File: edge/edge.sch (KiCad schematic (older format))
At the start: 13 parts

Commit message: edge boards
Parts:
- removed D? (x3): LED, ~, symbol LED
- removed R? (x3): R, ~, symbol R
- added C2, C3, C4, C6, C7, C8, C9: 0.1uF, ~, symbol C
- added C5: 2.2uF, ~, symbol C
- added L1: INDUCTOR, ~, symbol INDUCTOR
- added P3: CONN_5, ~, symbol CONN_5
- added P4: CONN_6, ~, symbol CONN_6
- added P5: CONN_3X2, ~, symbol CONN_3X2
- added R1, R2, R3: 22R, ~, symbol R
- gave numbers to parts that had none: 7
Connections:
- net labels added: MISO, MOSI, PA0, PA2, SCK, \RESET
- wire segments 42 -> 76
- no-connect marks 0 -> 4

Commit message: Last version before ATtiny24A
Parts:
- added R4, R5: 10K, ~, symbol R
- added R6, R7, R8: R, ~, symbol R
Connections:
- net labels added: BTN1, BTN1C, BTN2, BTN2C, PB2, PB4
- net labels removed: PA0
- wire segments 76 -> 89
- no-connect marks 4 -> 1

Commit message: ATtiny24A based edge board
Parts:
- removed C5: 2.2uF, ~, symbol C
- removed C6, C7, C8, C9: 0.1uF, ~, symbol C
- removed IC1: ATTINY861A-S, SO20, symbol ATTINY861A-S
- removed P4: CONN_6, ~, symbol CONN_6
- removed Q1, Q2, Q3: MOSFET_N, ~, symbol MOSFET_N
- removed R4, R5: 10K, ~, symbol R
- removed R8: R, ~, symbol R
- added IC1: ATTINY24A-SS, SO14, symbol ATTINY24A-SS
- added Q1, Q2, Q3: NPN, ~, symbol NPN
- added R3: 10K, ~, symbol R
- C2, C4: value 0.1uF -> 10uF
- C3: value 0.1uF -> 1uF
- R1: value 22R -> 170R
- R4: renamed from R2; value 22R -> 170R
- R6, R7: value R -> 10K
- R8: renamed from R3; value 22R -> 170R
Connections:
- net labels added: BB, BLUEP, GB, GREENP, RB, REDP
- net labels removed: PA2, PB2, PB4
- wire segments 89 -> 71
- no-connect marks 1 -> 0

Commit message: Game of Life edge board rerouting
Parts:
- added C5, C6: C, ~, symbol C
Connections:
- wire segments 71 -> 78
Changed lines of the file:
@@
-EESchema Schematic File Version 2  date Sun 05 May 2013 09:03:02 PM EDT
+EESchema Schematic File Version 2  date Sat 11 May 2013 07:52:54 PM EDT
 LIBS:power
 LIBS:device
@@
 Sheet 1 1
 Title ""
-Date "6 may 2013"
+Date "11 may 2013"
 Rev ""
 Comp ""
@@
 $EndComp
 $Comp
-L GND #PWR01
+L GND #PWR10
 U 1 1 512EAE5B
 P 3700 5100
-F 0 "#PWR01" H 3700 5100 30  0001 C CNN
+F 0 "#PWR10" H 3700 5100 30  0001 C CNN
 F 1 "GND" H 3700 5030 30  0001 C CNN
 F 2 "" H 3700 5100 60  0000 C CNN
@@
 $EndComp
 $Comp
-L +3.3V #PWR02
+L +3.3V #PWR12
 U 1 1 512EAE7E
 P 3800 4900
-F 0 "#PWR02" H 3800 4860 30  0001 C CNN
+F 0 "#PWR12" H 3800 4860 30  0001 C CNN
 F 1 "+3.3V" H 3800 5010 30  0000 C CNN
 F 2 "" H 3800 4900 60  0000 C CNN
@@
 $EndComp
 $Comp
-L +12V #PWR03
+L +12V #PWR11
 U 1 1 512EAEA3
 P 3800 4800
-F 0 "#PWR03" H 3800 4750 20  0001 C CNN
+F 0 "#PWR11" H 3800 4750 20  0001 C CNN
 F 1 "+12V" H 3800 4900 30  0000 C CNN
 F 2 "" H 3800 4800 60  0000 C CNN
@@
 $EndComp
 $Comp
-L GND #PWR04
+L GND #PWR17
 U 1 1 512EAF89
 P 4750 5150
-F 0 "#PWR04" H 4750 5150 30  0001 C CNN
+F 0 "#PWR17" H 4750 5150 30  0001 C CNN
 F 1 "GND" H 4750 5080 30  0001 C CNN
 F 2 "" H 4750 5150 60  0000 C CNN
@@
 $EndComp
 $Comp
-L +3.3V #PWR05
+L +3.3V #PWR20
 U 1 1 512EAF91
 P 4850 4950
-F 0 "#PWR05" H 4850 4910 30  0001 C CNN
+F 0 "#PWR20" H 4850 4910 30  0001 C CNN
 F 1 "+3.3V" H 4850 5060 30  0000 C CNN
 F 2 "" H 4850 4950 60  0000 C CNN
@@
 $EndComp
 $Comp
-L +12V #PWR06
+L +12V #PWR19
 U 1 1 512EAF98
 P 4850 4850
-F 0 "#PWR06" H 4850 4800 20  0001 C CNN
+F 0 "#PWR19" H 4850 4800 20  0001 C CNN
 F 1 "+12V" H 4850 4950 30  0000 C CNN
 F 2 "" H 4850 4850 60  0000 C CNN
@@
 INCCW2
 $Comp
-L GND #PWR07
+L GND #PWR9
 U 1 1 512EB1D0
 P 3550 7200
-F 0 "#PWR07" H 3550 7200 30  0001 C CNN
+F 0 "#PWR9" H 3550 7200 30  0001 C CNN
 F 1 "GND" H 3550 7130 30  0001 C CNN
 F 2 "" H 3550 7200 60  0000 C CNN
@@
 RED
 $Comp
-L GND #PWR08
+L GND #PWR15
 U 1 1 512EB27D
 P 4300 7200
-F 0 "#PWR08" H 4300 7200 30  0001 C CNN
+F 0 "#PWR15" H 4300 7200 30  0001 C CNN
 F 1 "GND" H 4300 7130 30  0001 C CNN
 F 2 "" H 4300 7200 60  0000 C CNN
@@
 $EndComp
 $Comp
-L GND #PWR09
+L GND #PWR21
 U 1 1 512EB2B8
 P 5250 7200
-F 0 "#PWR09" H 5250 7200 30  0001 C CNN
+F 0 "#PWR21" H 5250 7200 30  0001 C CNN
 F 1 "GND" H 5250 7130 30  0001 C CNN
 F 2 "" H 5250 7200 60  0000 C CNN
@@
 $EndComp
 $Comp
-L +12V #PWR010
+L +12V #PWR13
 U 1 1 5183CE12
 P 4000 5750
-F 0 "#PWR010" H 4000 5700 20  0001 C CNN
+F 0 "#PWR13" H 4000 5700 20  0001 C CNN
 F 1 "+12V" H 4000 5850 30  0000 C CNN
 F 2 "" H 4000 5750 60  0000 C CNN
@@
 $EndComp
 $Comp
-L +12V #PWR011
+L +12V #PWR16
 U 1 1 5183E9DB
 P 4700 5750
-F 0 "#PWR011" H 4700 5700 20  0001 C CNN
+F 0 "#PWR16" H 4700 5700 20  0001 C CNN
 F 1 "+12V" H 4700 5850 30  0000 C CNN
 F 2 "" H 4700 5750 60  0000 C CNN
@@
 $EndComp
 $Comp
-L VCC #PWR012
+L VCC #PWR2
 U 1 1 5186E69A
 P 1300 900
-F 0 "#PWR012" H 1300 1000 30  0001 C CNN
+F 0 "#PWR2" H 1300 1000 30  0001 C CNN
 F 1 "VCC" H 1300 1000 30  0000 C CNN
 F 2 "" H 1300 900 60  0000 C CNN
@@
 $EndComp
 $Comp
-L GND #PWR013
+L GND #PWR3
 U 1 1 5186E6E5
 P 1300 2300
-F 0 "#PWR013" H 1300 2300 30  0001 C CNN
+F 0 "#PWR3" H 1300 2300 30  0001 C CNN
 F 1 "GND" H 1300 2230 30  0001 C CNN
 F 2 "" H 1300 2300 60  0000 C CNN
@@
 $EndComp
 $Comp
-L GND #PWR014
+L GND #PWR1
 U 1 1 5186F52B
 P 700 1000
-F 0 "#PWR014" H 700 1000 30  0001 C CNN
+F 0 "#PWR1" H 700 1000 30  0001 C CNN
 F 1 "GND" H 700 930 30  0001 C CNN
 F 2 "" H 700 1000 60  0000 C CNN
@@
 $EndComp
 $Comp
-L VCC #PWR015
+L VCC #PWR14
 U 1 1 51870416
 P 4200 2400
-F 0 "#PWR015" H 4200 2500 30  0001 C CNN
+F 0 "#PWR14" H 4200 2500 30  0001 C CNN
 F 1 "VCC" H 4200 2500 30  0000 C CNN
 F 2 "" H 4200 2400 60  0000 C CNN
@@
 $EndComp
 $Comp
-L +3.3V #PWR016
+L +3.3V #PWR4
 U 1 1 518704B9
 P 1400 900
-F 0 "#PWR016" H 1400 860 30  0001 C CNN
+F 0 "#PWR4" H 1400 860 30  0001 C CNN
 F 1 "+3.3V" H 1400 1010 30  0000 C CNN
 F 2 "" H 1400 900 60  0000 C CNN
@@
 $EndComp
 $Comp
-L GND #PWR017
+L GND #PWR18
 U 1 1 518453AF
 P 4850 2300
-F 0 "#PWR017" H 4850 2300 30  0001 C CNN
+F 0 "#PWR18" H 4850 2300 30  0001 C CNN
 F 1 "GND" H 4850 2230 30  0001 C CNN
 F 2 "" H 4850 2300 60  0000 C CNN
@@
 $EndComp
 $Comp
-L VCC #PWR018
+L VCC #PWR5
 U 1 1 51870136
 P 2500 2850
-F 0 "#PWR018" H 2500 2950 30  0001 C CNN
+F 0 "#PWR5" H 2500 2950 30  0001 C CNN
 F 1 "VCC" H 2500 2950 30  0000 C CNN
 F 2 "" H 2500 2850 60  0000 C CNN
@@
 	2500 2850 2500 2950
 $Comp
-L GND #PWR019
+L GND #PWR6
 U 1 1 51870190
 P 2500 3450
-F 0 "#PWR019" H 2500 3450 30  0001 C CNN
+F 0 "#PWR6" H 2500 3450 30  0001 C CNN
 F 1 "GND" H 2500 3380 30  0001 C CNN
 F 2 "" H 2500 3450 60  0000 C CNN
@@
 	2500 3450 2500 3350
 $Comp
-L +12V #PWR020
+L +12V #PWR7
 U 1 1 5187029F
 P 2900 2850
-F 0 "#PWR020" H 2900 2800 20  0001 C CNN
+F 0 "#PWR7" H 2900 2800 20  0001 C CNN
 F 1 "+12V" H 2900 2950 30  0000 C CNN
 F 2 "" H 2900 2850 60  0000 C CNN
@@
 	2900 2950 2900 2850
 $Comp
-L GND #PWR021
+L GND #PWR8
 U 1 1 5187030A
 P 2900 3450
-F 0 "#PWR021" H 2900 3450 30  0001 C CNN
+F 0 "#PWR8" H 2900 3450 30  0001 C CNN
 F 1 "GND" H 2900 3380 30  0001 C CNN
 F 2 "" H 2900 3450 60  0000 C CNN
@@
 Wire Wire Line
 	2900 3450 2900 3350
+Wire Wire Line
+	4600 1000 5150 1000
+Wire Wire Line
+	4600 1100 5150 1100
+$Comp
+L C C5
+U 1 1 518ECCE5
+P 4900 1350
+F 0 "C5" H 4900 1450 40  0000 L CNN
+F 1 "C" H 4906 1265 40  0000 L CNN
+F 2 "~" H 4938 1200 30  0000 C CNN
+F 3 "~" H 4900 1350 60  0000 C CNN
+	1    4900 1350
+	1    0    0    -1
+$EndComp
+$Comp
+L C C6
+U 1 1 518ECCF4
+P 5100 1350
+F 0 "C6" H 5100 1450 40  0000 L CNN
+F 1 "C" H 5106 1265 40  0000 L CNN
+F 2 "~" H 5138 1200 30  0000 C CNN
+F 3 "~" H 5100 1350 60  0000 C CNN
+	1    5100 1350
+	1    0    0    -1
+$EndComp
+$Comp
+L GND #PWR22
+U 1 1 518ECD03
+P 5300 1600
+F 0 "#PWR22" H 5300 1600 30  0001 C CNN
+F 1 "GND" H 5300 1530 30  0001 C CNN
+F 2 "" H 5300 1600 60  0000 C CNN
+F 3 "" H 5300 1600 60  0000 C CNN
+	1    5300 1600
+	0    -1   -1   0
+$EndComp
+Wire Wire Line
+	5300 1600 4900 1600
+Wire Wire Line
+	4900 1600 4900 1550
+Wire Wire Line
+	5100 1550 5100 1600
+Connection ~ 5100 1600
+Wire Wire Line
+	4900 1150 4900 1000
+Connection ~ 4900 1000
+Wire Wire Line
+	5100 1100 5100 1150
+Connection ~ 5100 1100
 $EndSCHEMATC

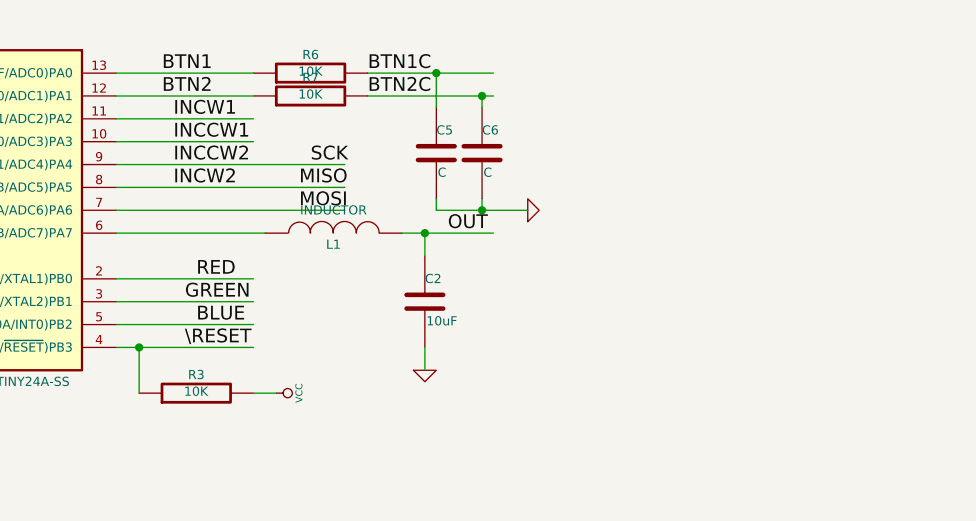
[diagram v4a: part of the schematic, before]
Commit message: Only one cap button, add LED to Game of Life edge boards
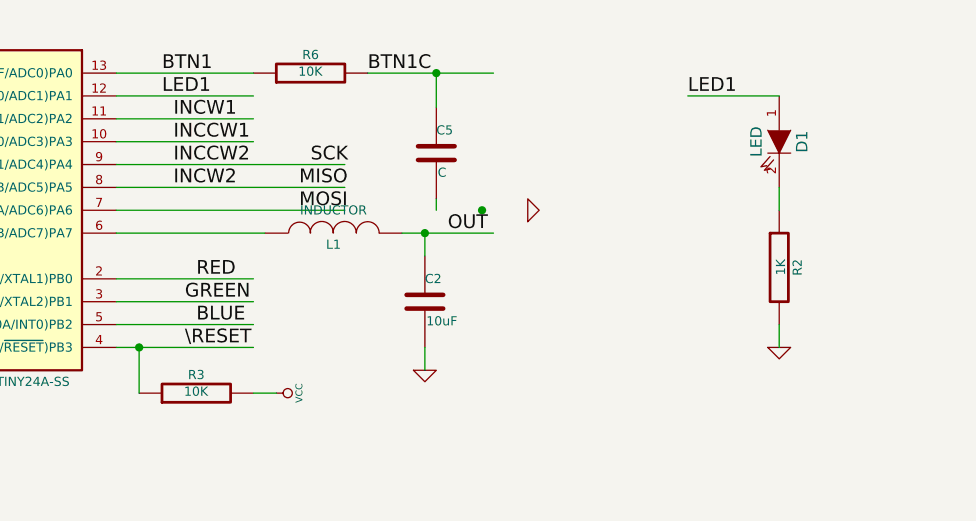
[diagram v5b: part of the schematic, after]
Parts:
- removed C6: C, ~, symbol C
- removed R7: 10K, ~, symbol R
- added D1: LED, ~, symbol LED
- added R2: 1K, ~, symbol R
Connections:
- net labels added: LED1
- net labels removed: BTN2, BTN2C
- wire segments 78 -> 77
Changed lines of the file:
@@
-EESchema Schematic File Version 2  date Sat 11 May 2013 07:52:54 PM EDT
+EESchema Schematic File Version 2  date Fri 10 May 2013 08:07:58 PM EDT
 LIBS:power
 LIBS:device
@@
 Sheet 1 1
 Title ""
-Date "11 may 2013"
+Date "10 may 2013"
 Rev ""
 Comp ""
@@
 $EndComp
 $Comp
-L GND #PWR10
+L GND #PWR01
 U 1 1 512EAE5B
 P 3700 5100
-F 0 "#PWR10" H 3700 5100 30  0001 C CNN
+F 0 "#PWR01" H 3700 5100 30  0001 C CNN
 F 1 "GND" H 3700 5030 30  0001 C CNN
 F 2 "" H 3700 5100 60  0000 C CNN
@@
 $EndComp
 $Comp
-L +3.3V #PWR12
+L +3.3V #PWR02
 U 1 1 512EAE7E
 P 3800 4900
-F 0 "#PWR12" H 3800 4860 30  0001 C CNN
+F 0 "#PWR02" H 3800 4860 30  0001 C CNN
 F 1 "+3.3V" H 3800 5010 30  0000 C CNN
 F 2 "" H 3800 4900 60  0000 C CNN
@@
 $EndComp
 $Comp
-L +12V #PWR11
+L +12V #PWR03
 U 1 1 512EAEA3
 P 3800 4800
-F 0 "#PWR11" H 3800 4750 20  0001 C CNN
+F 0 "#PWR03" H 3800 4750 20  0001 C CNN
 F 1 "+12V" H 3800 4900 30  0000 C CNN
 F 2 "" H 3800 4800 60  0000 C CNN
@@
 $EndComp
 $Comp
-L GND #PWR17
+L GND #PWR04
 U 1 1 512EAF89
 P 4750 5150
-F 0 "#PWR17" H 4750 5150 30  0001 C CNN
+F 0 "#PWR04" H 4750 5150 30  0001 C CNN
 F 1 "GND" H 4750 5080 30  0001 C CNN
 F 2 "" H 4750 5150 60  0000 C CNN
@@
 $EndComp
 $Comp
-L +3.3V #PWR20
+L +3.3V #PWR05
 U 1 1 512EAF91
 P 4850 4950
-F 0 "#PWR20" H 4850 4910 30  0001 C CNN
+F 0 "#PWR05" H 4850 4910 30  0001 C CNN
 F 1 "+3.3V" H 4850 5060 30  0000 C CNN
 F 2 "" H 4850 4950 60  0000 C CNN
@@
 $EndComp
 $Comp
-L +12V #PWR19
+L +12V #PWR06
 U 1 1 512EAF98
 P 4850 4850
-F 0 "#PWR19" H 4850 4800 20  0001 C CNN
+F 0 "#PWR06" H 4850 4800 20  0001 C CNN
 F 1 "+12V" H 4850 4950 30  0000 C CNN
 F 2 "" H 4850 4850 60  0000 C CNN
@@
 INCCW2
 $Comp
-L GND #PWR9
+L GND #PWR07
 U 1 1 512EB1D0
 P 3550 7200
-F 0 "#PWR9" H 3550 7200 30  0001 C CNN
+F 0 "#PWR07" H 3550 7200 30  0001 C CNN
 F 1 "GND" H 3550 7130 30  0001 C CNN
 F 2 "" H 3550 7200 60  0000 C CNN
@@
 RED
 $Comp
-L GND #PWR15
+L GND #PWR08
 U 1 1 512EB27D
 P 4300 7200
-F 0 "#PWR15" H 4300 7200 30  0001 C CNN
+F 0 "#PWR08" H 4300 7200 30  0001 C CNN
 F 1 "GND" H 4300 7130 30  0001 C CNN
 F 2 "" H 4300 7200 60  0000 C CNN
@@
 $EndComp
 $Comp
-L GND #PWR21
+L GND #PWR09
 U 1 1 512EB2B8
 P 5250 7200
-F 0 "#PWR21" H 5250 7200 30  0001 C CNN
+F 0 "#PWR09" H 5250 7200 30  0001 C CNN
 F 1 "GND" H 5250 7130 30  0001 C CNN
 F 2 "" H 5250 7200 60  0000 C CNN
@@
 $EndComp
 $Comp
-L +12V #PWR13
+L +12V #PWR010
 U 1 1 5183CE12
 P 4000 5750
-F 0 "#PWR13" H 4000 5700 20  0001 C CNN
+F 0 "#PWR010" H 4000 5700 20  0001 C CNN
 F 1 "+12V" H 4000 5850 30  0000 C CNN
 F 2 "" H 4000 5750 60  0000 C CNN
@@
 $EndComp
 $Comp
-L +12V #PWR16
+L +12V #PWR011
 U 1 1 5183E9DB
 P 4700 5750
-F 0 "#PWR16" H 4700 5700 20  0001 C CNN
+F 0 "#PWR011" H 4700 5700 20  0001 C CNN
 F 1 "+12V" H 4700 5850 30  0000 C CNN
 F 2 "" H 4700 5750 60  0000 C CNN
@@
 $EndComp
 $Comp
-L VCC #PWR2
+L VCC #PWR012
 U 1 1 5186E69A
 P 1300 900
-F 0 "#PWR2" H 1300 1000 30  0001 C CNN
+F 0 "#PWR012" H 1300 1000 30  0001 C CNN
 F 1 "VCC" H 1300 1000 30  0000 C CNN
 F 2 "" H 1300 900 60  0000 C CNN
@@
 $EndComp
 $Comp
-L GND #PWR3
+L GND #PWR013
 U 1 1 5186E6E5
 P 1300 2300
-F 0 "#PWR3" H 1300 2300 30  0001 C CNN
+F 0 "#PWR013" H 1300 2300 30  0001 C CNN
 F 1 "GND" H 1300 2230 30  0001 C CNN
 F 2 "" H 1300 2300 60  0000 C CNN
@@
 $EndComp
 $Comp
-L GND #PWR1
+L GND #PWR014
 U 1 1 5186F52B
 P 700 1000
-F 0 "#PWR1" H 700 1000 30  0001 C CNN
+F 0 "#PWR014" H 700 1000 30  0001 C CNN
 F 1 "GND" H 700 930 30  0001 C CNN
 F 2 "" H 700 1000 60  0000 C CNN
@@
 $EndComp
 $Comp
-L VCC #PWR14
+L VCC #PWR015
 U 1 1 51870416
 P 4200 2400
-F 0 "#PWR14" H 4200 2500 30  0001 C CNN
+F 0 "#PWR015" H 4200 2500 30  0001 C CNN
 F 1 "VCC" H 4200 2500 30  0000 C CNN
 F 2 "" H 4200 2400 60  0000 C CNN
@@
 $EndComp
 $Comp
-L +3.3V #PWR4
+L +3.3V #PWR016
 U 1 1 518704B9
 P 1400 900
-F 0 "#PWR4" H 1400 860 30  0001 C CNN
+F 0 "#PWR016" H 1400 860 30  0001 C CNN
 F 1 "+3.3V" H 1400 1010 30  0000 C CNN
 F 2 "" H 1400 900 60  0000 C CNN
@@
 Text Label 3700 1000 0    60   ~ 0
 BTN1
-Wire Wire Line
-	3500 1100 4100 1100
-Text Label 3700 1100 0    60   ~ 0
-BTN2
 $Comp
 L R R6
@@
 	0    -1   -1   0
 $EndComp
-$Comp
-L R R7
-U 1 1 51873C58
-P 4350 1100
-F 0 "R7" V 4430 1100 40  0000 C CNN
-F 1 "10K" V 4357 1101 40  0000 C CNN
-F 2 "~" V 4280 1100 30  0000 C CNN
-F 3 "~" H 4350 1100 30  0000 C CNN
-	1    4350 1100
-	0    -1   -1   0
-$EndComp
 Text Label 4600 1000 0    60   ~ 0
 BTN1C
-Text Label 4600 1100 0    60   ~ 0
-BTN2C
 Wire Wire Line
 	3500 1200 4100 1200
@@
 $EndComp
 $Comp
-L GND #PWR18
+L GND #PWR017
 U 1 1 518453AF
 P 4850 2300
-F 0 "#PWR18" H 4850 2300 30  0001 C CNN
+F 0 "#PWR017" H 4850 2300 30  0001 C CNN
 F 1 "GND" H 4850 2230 30  0001 C CNN
 F 2 "" H 4850 2300 60  0000 C CNN
@@
 $EndComp
 $Comp
-L VCC #PWR5
+L VCC #PWR018
 U 1 1 51870136
 P 2500 2850
-F 0 "#PWR5" H 2500 2950 30  0001 C CNN
+F 0 "#PWR018" H 2500 2950 30  0001 C CNN
 F 1 "VCC" H 2500 2950 30  0000 C CNN
 F 2 "" H 2500 2850 60  0000 C CNN
@@
 	2500 2850 2500 2950
 $Comp
-L GND #PWR6
+L GND #PWR019
 U 1 1 51870190
 P 2500 3450
-F 0 "#PWR6" H 2500 3450 30  0001 C CNN
+F 0 "#PWR019" H 2500 3450 30  0001 C CNN
 F 1 "GND" H 2500 3380 30  0001 C CNN
 F 2 "" H 2500 3450 60  0000 C CNN
@@
 	2500 3450 2500 3350
 $Comp
-L +12V #PWR7
+L +12V #PWR020
 U 1 1 5187029F
 P 2900 2850
-F 0 "#PWR7" H 2900 2800 20  0001 C CNN
+F 0 "#PWR020" H 2900 2800 20  0001 C CNN
 F 1 "+12V" H 2900 2950 30  0000 C CNN
 F 2 "" H 2900 2850 60  0000 C CNN
@@
 	2900 2950 2900 2850
 $Comp
-L GND #PWR8
+L GND #PWR021
 U 1 1 5187030A
 P 2900 3450
-F 0 "#PWR8" H 2900 3450 30  0001 C CNN
+F 0 "#PWR021" H 2900 3450 30  0001 C CNN
 F 1 "GND" H 2900 3380 30  0001 C CNN
 F 2 "" H 2900 3450 60  0000 C CNN
@@
 Wire Wire Line
 	2900 3450 2900 3350
+$Comp
+L GND #PWR022
+U 1 1 518ECD03
+P 5300 1600
+F 0 "#PWR022" H 5300 1600 30  0001 C CNN
+F 1 "GND" H 5300 1530 30  0001 C CNN
+F 2 "" H 5300 1600 60  0000 C CNN
+F 3 "" H 5300 1600 60  0000 C CNN
+	1    5300 1600
+	0    -1   -1   0
+$EndComp
+Wire Wire Line
+	4900 1600 4900 1550
+Connection ~ 5100 1600
+Connection ~ 4900 1000
 Wire Wire Line
 	4600 1000 5150 1000
 Wire Wire Line
-	4600 1100 5150 1100
+	4900 1150 4900 1000
 $Comp
 L C C5
@@
 	1    0    0    -1
 $EndComp
-$Comp
-L C C6
-U 1 1 518ECCF4
-P 5100 1350
-F 0 "C6" H 5100 1450 40  0000 L CNN
-F 1 "C" H 5106 1265 40  0000 L CNN
-F 2 "~" H 5138 1200 30  0000 C CNN
-F 3 "~" H 5100 1350 60  0000 C CNN
-	1    5100 1350
-	1    0    0    -1
-$EndComp
-$Comp
-L GND #PWR22
-U 1 1 518ECD03
-P 5300 1600
-F 0 "#PWR22" H 5300 1600 30  0001 C CNN
-F 1 "GND" H 5300 1530 30  0001 C CNN
-F 2 "" H 5300 1600 60  0000 C CNN
-F 3 "" H 5300 1600 60  0000 C CNN
-	1    5300 1600
-	0    -1   -1   0
-$EndComp
-Wire Wire Line
-	5300 1600 4900 1600
-Wire Wire Line
-	4900 1600 4900 1550
-Wire Wire Line
-	5100 1550 5100 1600
-Connection ~ 5100 1600
-Wire Wire Line
-	4900 1150 4900 1000
-Connection ~ 4900 1000
-Wire Wire Line
-	5100 1100 5100 1150
-Connection ~ 5100 1100
+Wire Wire Line
+	3500 1100 4100 1100
+Text Label 3700 1100 0    60   ~ 0
+LED1
+$Comp
+L LED D1
+U 1 1 518D44B0
+P 6400 1300
+F 0 "D1" H 6400 1400 50  0000 C CNN
+F 1 "LED" H 6400 1200 50  0000 C CNN
+F 2 "~" H 6400 1300 60  0000 C CNN
+F 3 "~" H 6400 1300 60  0000 C CNN
+	1    6400 1300
+	0    1    1    0
+$EndComp
+$Comp
+L R R2
+U 1 1 518D44BF
+P 6400 1850
+F 0 "R2" V 6480 1850 40  0000 C CNN
+F 1 "1K" V 6407 1851 40  0000 C CNN
+F 2 "~" V 6330 1850 30  0000 C CNN
+F 3 "~" H 6400 1850 30  0000 C CNN
+	1    6400 1850
+	1    0    0    -1
+$EndComp
+$Comp
+L GND #PWR023
+U 1 1 518D44D3
+P 6400 2200
+F 0 "#PWR023" H 6400 2200 30  0001 C CNN
+F 1 "GND" H 6400 2130 30  0001 C CNN
+F 2 "" H 6400 2200 60  0000 C CNN
+F 3 "" H 6400 2200 60  0000 C CNN
+	1    6400 2200
+	1    0    0    -1
+$EndComp
+Wire Wire Line
+	6400 2200 6400 2100
+Wire Wire Line
+	6400 1600 6400 1500
+Wire Wire Line
+	6400 1100 6000 1100
+Text Label 6000 1100 0    60   ~ 0
+LED1
 $EndSCHEMATC

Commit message: Hack Manhattan Color Life boards final version
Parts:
- L1: value INDUCTOR -> 1K
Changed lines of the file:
@@
-EESchema Schematic File Version 2  date Fri 10 May 2013 08:07:58 PM EDT
+EESchema Schematic File Version 2
 LIBS:power
 LIBS:device
@@
 P 4450 1700
 F 0 "L1" V 4400 1700 40  0000 C CNN
-F 1 "INDUCTOR" V 4550 1700 40  0000 C CNN
+F 1 "1K" V 4400 1550 40  0000 C CNN
 F 2 "~" H 4450 1700 60  0000 C CNN
 F 3 "~" H 4450 1700 60  0000 C CNN
